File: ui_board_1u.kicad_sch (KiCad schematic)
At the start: 38 parts, among them J1 X9555WV-2x06-6TV01, U1 AFC01-S30FCA-00, U2 SPX3819M5-L, U3 TPS61040DBV

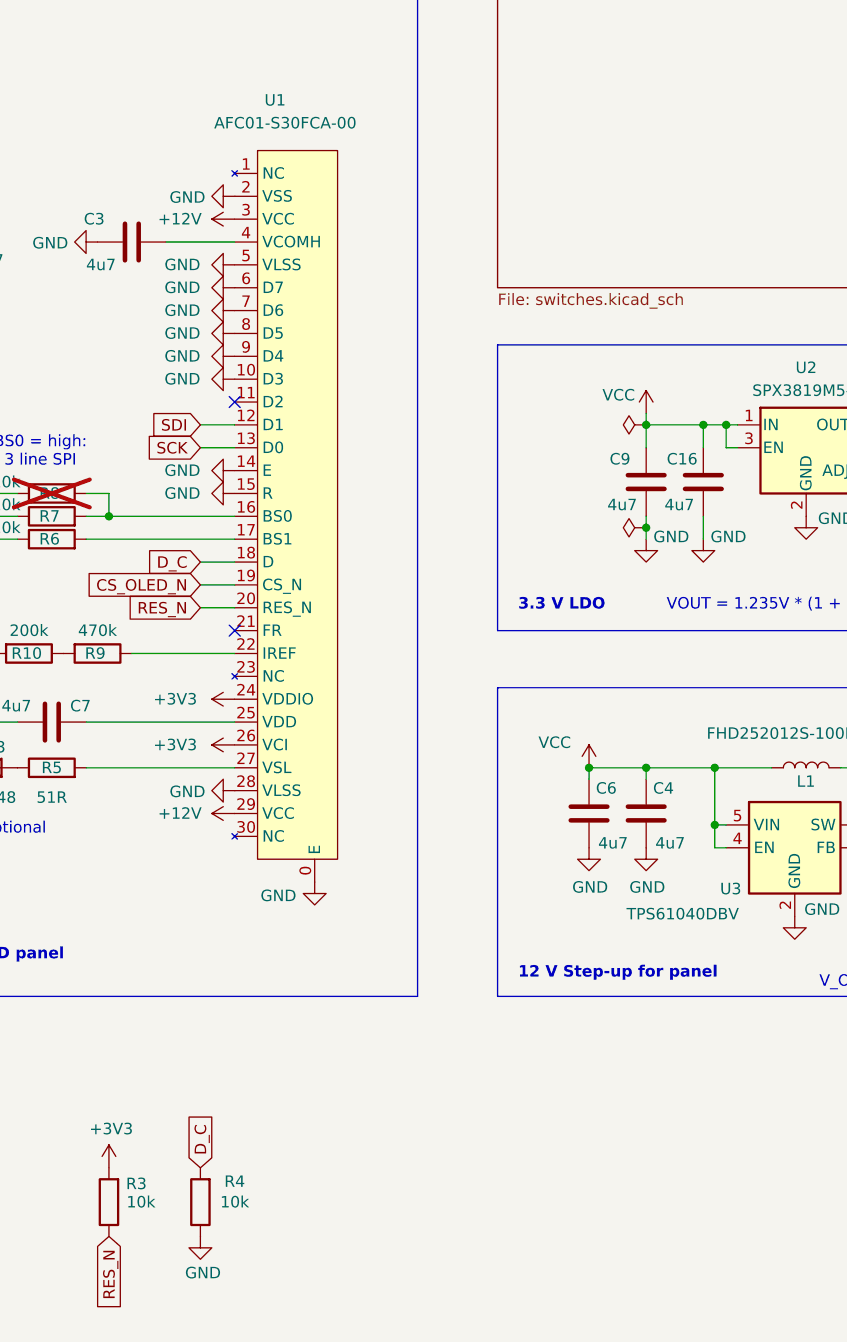
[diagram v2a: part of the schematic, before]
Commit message: review OLED pinout, add 2 GND pins
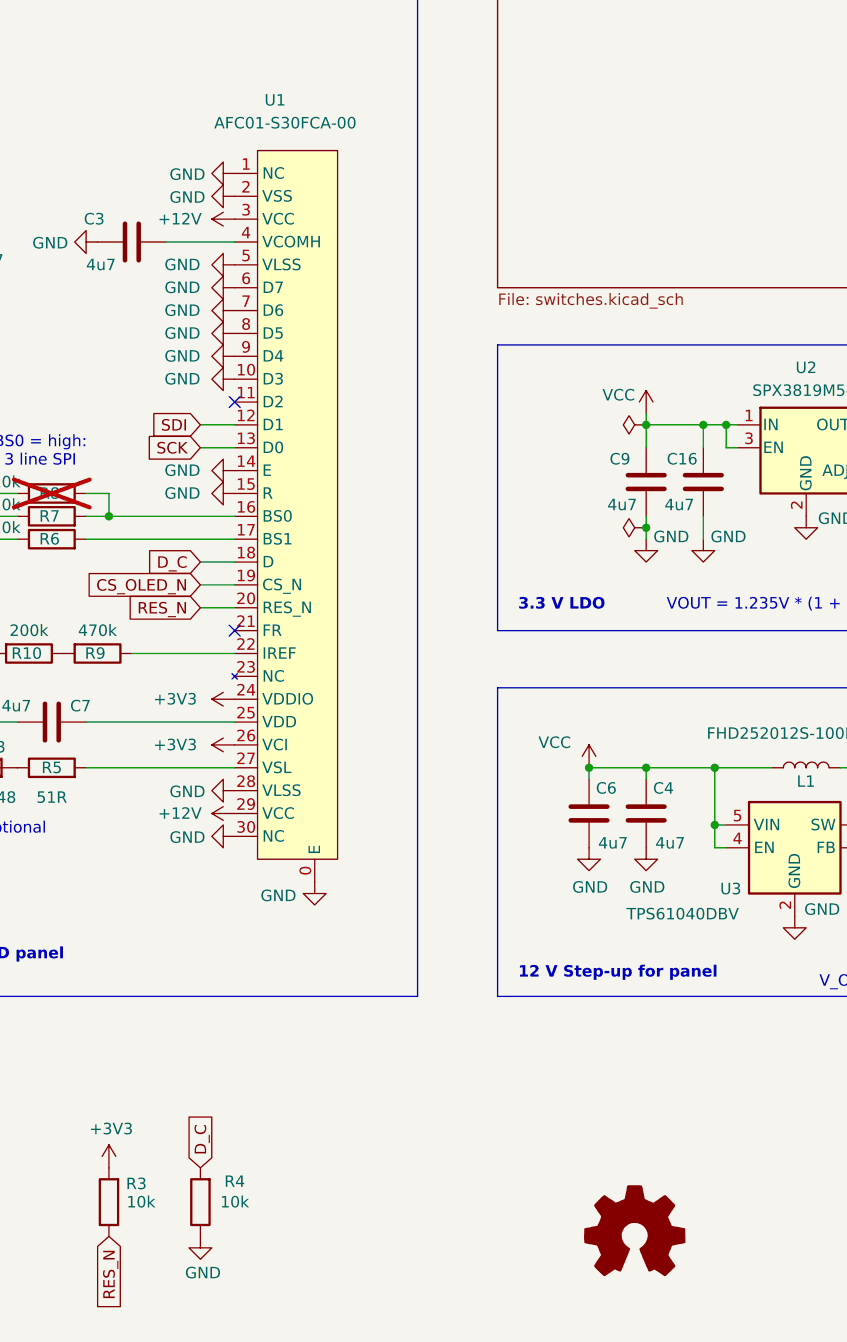
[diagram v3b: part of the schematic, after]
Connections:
- net GND: now also U1.1 (NC), U1.30 (NC)
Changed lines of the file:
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@@
 	(title_block
 		(title "ui_board_1u - User interface board")
-		(date "2025-12-07")
+		(date "2025-12-17")
 		(rev "-")
 		(company "Betz Engineering")
@@
 	)
 	(image
-		(at 182.88 172.72)
+		(at 187.325 172.085)
 		(scale 0.417576)
 		(data "iVBORw0KGgoAAAANSUhEUgAAAP4AAAD+CAYAAAAalrhRAAAACXBIWXMAAC4jAAAuIwF4pT92AAAA"
@@
 	(symbol
 		(lib_id "power:GND")
+		(at 158.75 128.27 270)
+		(unit 1)
+		(exclude_from_sim no)
+		(in_bom yes)
+		(on_board yes)
+		(dnp no)
+		(property "Reference" "#PWR014"
+			(at 152.4 128.27 0)
+			(effects
+				(font
+					(size 1.27 1.27)
+				)
+				(hide yes)
+			)
+		)
+		(property "Value" "GND"
+			(at 155.4988 128.397 90)
+			(effects
+				(font
+					(size 1.27 1.27)
+				)
+				(justify right)
+			)
+		)
+		(property "Footprint" ""
+			(at 158.75 128.27 0)
+			(effects
+				(font
+					(size 1.27 1.27)
+				)
+				(hide yes)
+			)
+		)
+		(property "Datasheet" ""
+			(at 158.75 128.27 0)
+			(effects
+				(font
+					(size 1.27 1.27)
+				)
+				(hide yes)
+			)
+		)
+		(property "Description" ""
+			(at 158.75 128.27 0)
+			(effects
+				(font
+					(size 1.27 1.27)
+				)
+			)
+		)
+		(pin "1"
+		)
+		(instances
+			(project "ui_board_1u"
+				(path "/3def8ca7-c7ff-40fd-acc8-d6d3f6c3eb5b"
+					(reference "#PWR014")
+					(unit 1)
+				)
+			)
+		)
+	)
+	(symbol
+		(lib_id "power:GND")
 		(at 167.64 133.35 0)
 		(unit 1)
@@
 	)
 	(symbol
+		(lib_id "power:GND")
+		(at 158.75 54.61 270)
+		(unit 1)
+		(exclude_from_sim no)
+		(in_bom yes)
+		(on_board yes)
+		(dnp no)
+		(property "Reference" "#PWR013"
+			(at 152.4 54.61 0)
+			(effects
+				(font
+					(size 1.27 1.27)
+				)
+				(hide yes)
+			)
+		)
+		(property "Value" "GND"
+			(at 155.4988 54.737 90)
+			(effects
+				(font
+					(size 1.27 1.27)
+				)
+				(justify right)
+			)
+		)
+		(property "Footprint" ""
+			(at 158.75 54.61 0)
+			(effects
+				(font
+					(size 1.27 1.27)
+				)
+				(hide yes)
+			)
+		)
+		(property "Datasheet" ""
+			(at 158.75 54.61 0)
+			(effects
+				(font
+					(size 1.27 1.27)
+				)
+				(hide yes)
+			)
+		)
+		(property "Description" ""
+			(at 158.75 54.61 0)
+			(effects
+				(font
+					(size 1.27 1.27)
+				)
+			)
+		)
+		(pin "1"
+		)
+		(instances
+			(project "ui_board_1u"
+				(path "/3def8ca7-c7ff-40fd-acc8-d6d3f6c3eb5b"
+					(reference "#PWR013")
+					(unit 1)
+				)
+			)
+		)
+	)
+	(symbol
 		(lib_id "Device:C")
 		(at 248.92 125.73 0)
@@
 					(unit 1)
 				)
+			)
+		)
+	)
+	(symbol
+		(lib_id "Graphic:Logo_Open_Hardware_Small")
+		(at 203.2 172.72 0)
+		(unit 1)
+		(exclude_from_sim yes)
+		(in_bom no)
+		(on_board no)
+		(dnp no)
+		(fields_autoplaced yes)
+		(property "Reference" "#SYM1"
+			(at 203.2 165.735 0)
+			(effects
+				(font
+					(size 1.27 1.27)
+				)
+				(hide yes)
+			)
+		)
+		(property "Value" "Logo_Open_Hardware_Small"
+			(at 203.2 178.435 0)
+			(effects
+				(font
+					(size 1.27 1.27)
+				)
+				(hide yes)
+			)
+		)
+		(property "Footprint" ""
+			(at 203.2 172.72 0)
+			(effects
+				(font
+					(size 1.27 1.27)
+				)
+				(hide yes)
+			)
+		)
+		(property "Datasheet" "~"
+			(at 203.2 172.72 0)
+			(effects
+				(font
+					(size 1.27 1.27)
+				)
+				(hide yes)
+			)
+		)
+		(property "Description" "Open Hardware logo, small"
+			(at 203.2 172.72 0)
+			(effects
+				(font
+					(size 1.27 1.27)
+				)
+				(hide yes)
+			)
+		)
+		(instances
+			(project ""
+				(path "/3def8ca7-c7ff-40fd-acc8-d6d3f6c3eb5b"
+					(reference "#SYM1")
+					(unit 1)
+				)

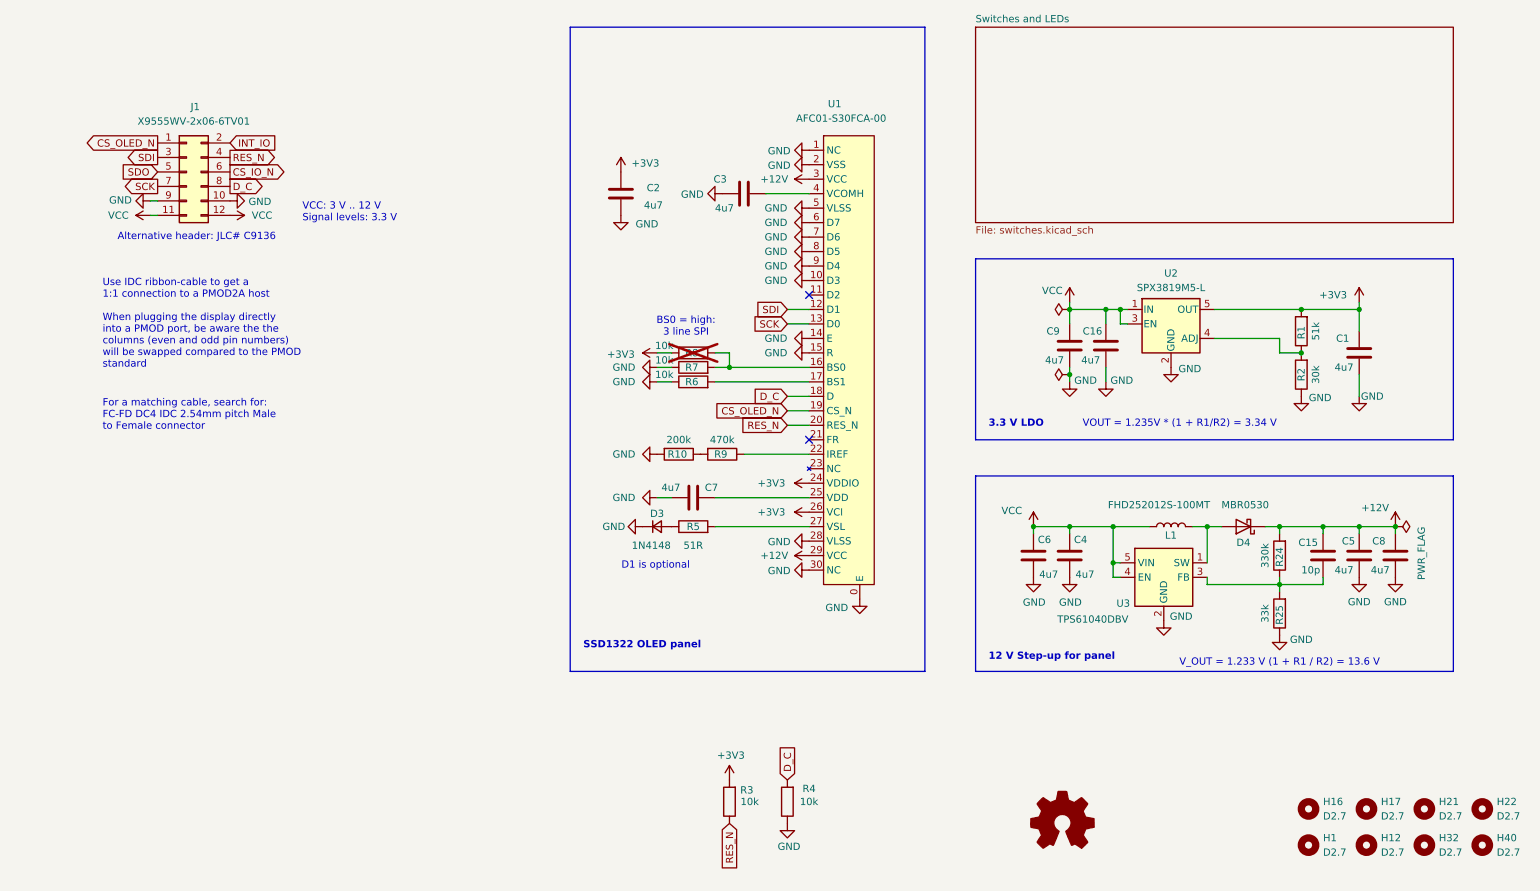
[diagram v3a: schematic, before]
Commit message: add extension board connector
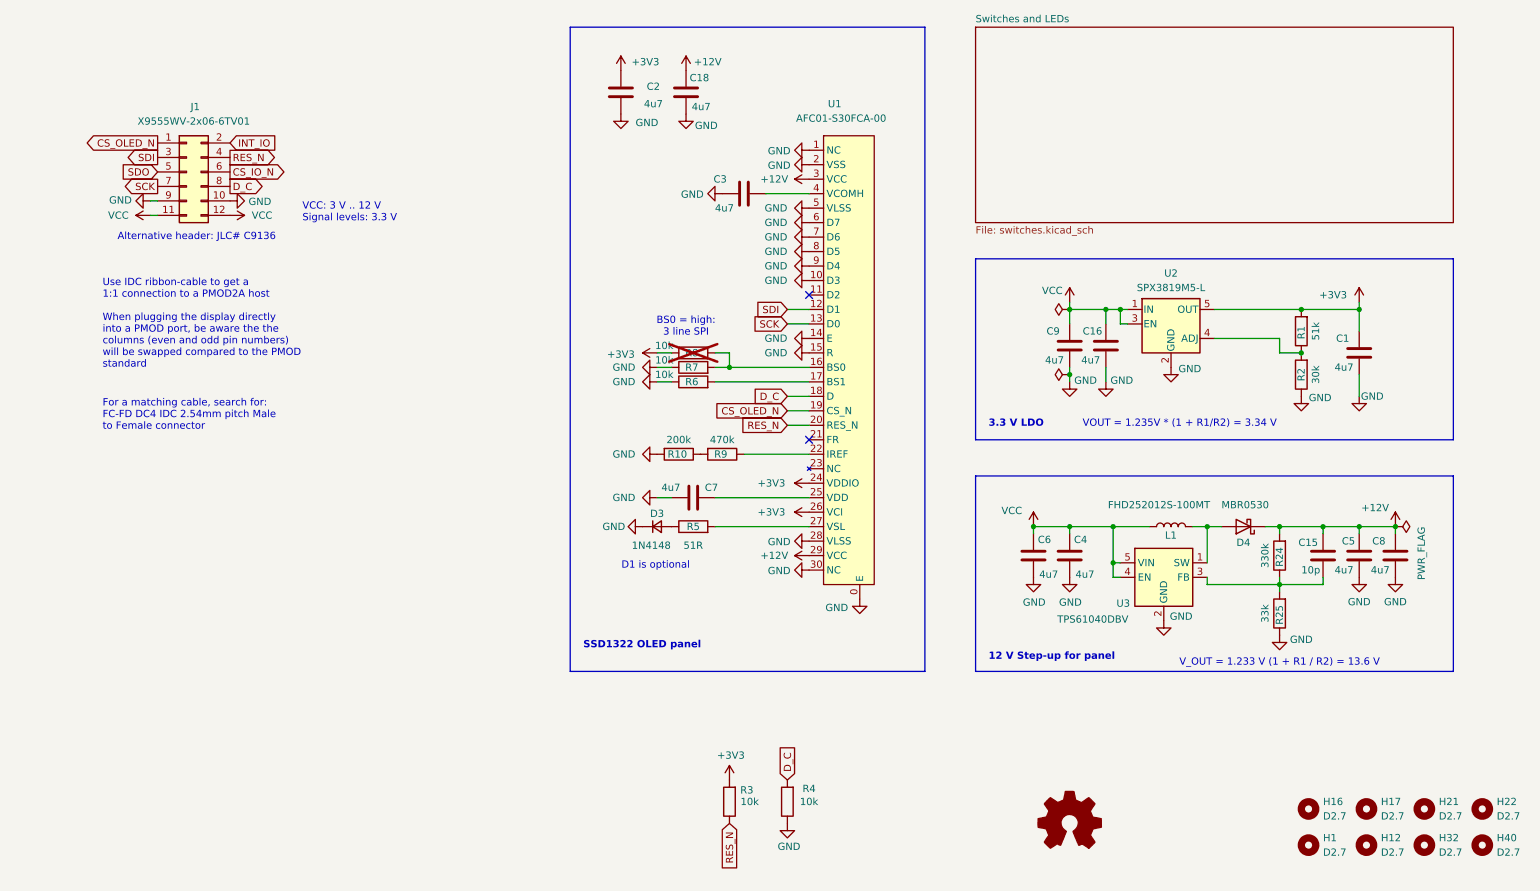
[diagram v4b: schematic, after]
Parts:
- added C18: 4u7, Capacitor_SMD:C_1206_3216Metric, symbol Device:C
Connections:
- net +12V: now also C18.1
- net GND: now also C18.2
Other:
- moved on the sheet: C2

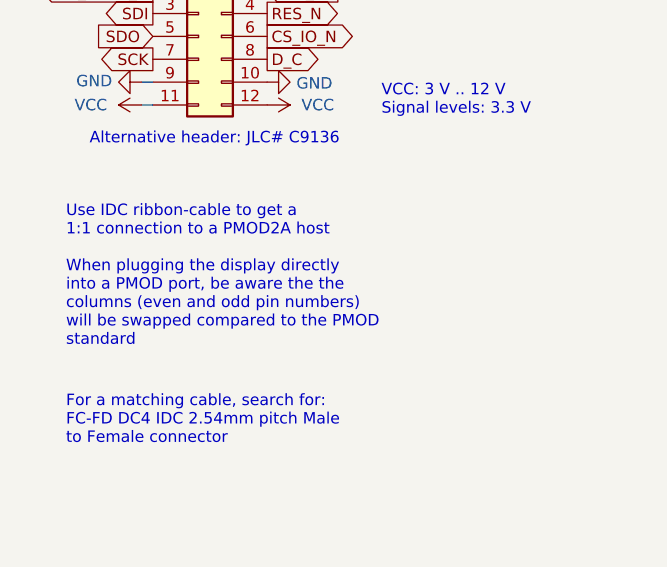
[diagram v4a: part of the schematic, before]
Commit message: fix typo in schematic
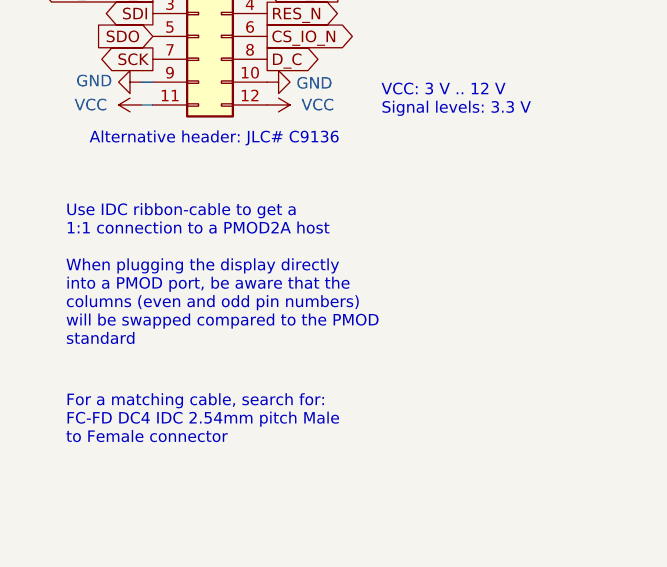
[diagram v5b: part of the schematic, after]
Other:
- note added: "Use IDC ribbon-cable to get a 1:1 connection to a PMOD2A host When plugging the display directly into a PMOD port, be aware that the columns (even and odd pin numbers) will be swapped compared to the PMOD standard"
- note removed: "Use IDC ribbon-cable to get a 1:1 connection to a PMOD2A host When plugging the display directly into a PMOD port, be aware the the columns (even and odd pin numbers) will be swapped compared to the PMOD standard"
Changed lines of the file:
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@@
 		)
 	)
-	(text "Use IDC ribbon-cable to get a \n1:1 connection to a PMOD2A host\n\nWhen plugging the display directly\ninto a PMOD port, be aware the the\ncolumns (even and odd pin numbers)\nwill be swapped compared to the PMOD\nstandard\n\n"
+	(text "Use IDC ribbon-cable to get a \n1:1 connection to a PMOD2A host\n\nWhen plugging the display directly\ninto a PMOD port, be aware that the\ncolumns (even and odd pin numbers)\nwill be swapped compared to the PMOD\nstandard\n\n"
 		(exclude_from_sim no)
 		(at 34.798 86.106 0)
@@
 			"vwAAAIAAAAAAAACAvwAUikCdUcXA3r+JPSuni0BersfA3r+JPSuni0CdUcXA3r+JPQAAAAAAAAAA"
 			"AACAvwAAAAAAAAAAAAAAAAAAAAAAAAAAAAAAAP///////////////wAAAIAAAACA3r+JPQIAAABx"
-			"vFjBAAAAAHeNog=="
-		)
-	)
+			"vFjBAAAAAHeNogAAAAAAAAAAAAAAAAAAAAAAAAAAAAAAAAAAAAAAAAAAAAAAAAAAAAAAAAAAAAAA"
+			"AAAAAAAAAAAAAAAAAAAAAAAAAAAAAAAAAAAAAAAAAAAAAAAAAAAAAAAAAAAAAAAAAAAAAAAAAAAA"
+			"AAAAAAAAAAAAAAAAAAAAAAAAAAAAAAAAAAAAAAAAAAAAAAAAAAAAAAAAAAAAAAAAAAAAAAAAAAAA"
+			"AAAAAAAAAAAAAAAAAAAAAAAAAAAAAAAAAAAAAAAAAAAAAAAAAAAAAAAAAAAAAAAAAAAAAAAAAAAA"
+			"AAAAAAAAAAAAAAAAAAAAAAAAAAAAAAAAAAAAAAAAAAAAAAAAAAAAAAAAAAAAAAAAAAAAAAAAAAAA"
+			"AAAAAAAAAAAAAAAAAAAAAAAAAAAAAAAAAAAAAAAAAAAAAAAAAAAAAAAAAAAAAAAAAAAAAAAAAAAA"
+			"AAAAAAAAAAAAAAAAAAAAAAAAAAAAAAAAAAAAAAAAAAAAAAAAAAAAAAAAAAAAAAAAAAAAAAAAAAAA"
+			"AAAAAAAAAAAAAAAAAAAAAAAAAAAAAAAAAAAAAAAAAAAAAAAAAAAAAAAAAAAAAAAAAAAAAAAAAAAA"
+			"AAAAAAAAAAAAAAAAAAAAAAAAAAAAAAAAAAAAAAAAAAAAAAAAAAAAAAAAAAAAAAAAAAAAAAAAAAAA"
+			"AAAAAAAAAAAAAAAAAAAAAAAAAAAAAAAAAAAAAAAAAAAAAAAAAAAAAAAAAAAAAAAAAAAAAAAAAAAA"
+			"AAAAAAAAAAAAAAAAAAAAAAAAAAAAAAAAAAAAAAAAAAAAAAAAAAAAAAAAAAAAAAAAAAAAAAAAAAAA"
+			"AAAAAAAAAAAAAAAAAAAAAAAAAAAAAAAAAAAAAAAAAAAAAAAAAAAAAAAAAAAAAAAAAAAAAAAAAAAA"
+			"AAAAAAAAAAAAAAAAAAAAAAAAAAAAAAAAAAAAAAAAAAAAAAAAAAAAAAAAAAAAAAAAAAAAAAAAAAAA"
+			"AAAAAAAAAAAAAAAAAAAAAAAAAAAAAAAAAAAAAAAAAAAAAAAAAAAAAAAAAAAAAAAAAAAAAAAAAAAA"
+			"AAAAAAAAAAAAAAAAAAAAAAAAAAAAAAAAAAAAAAAAAAAAAAAAAAAAAAAAAAAAAAAAAAAAAAAAAAAA"
+			"AAAAAAAAAAAAAAAAAAAAAAAAAAAAAAAAAAAAAAAAAAAAAAAAAAAAAAAAAAAAAAAAAAAAAAAAAAAA"
+			"AAAAAAAAAAAAAAAAAAAAAAAAAAAAAAAAAAAAAAAAAAAAAAAAAAAAAAAAAAAAAAAAAAAAAAAAAAAA"
+			"AAAAAAAAAAAAAAAAAAAAAAAAAAAAAAAAAAAAAAAAAAAAAAAAAAAAAAAAAAAAAAAAAAAAAAAAAAAA"
+			"AAAAAAAAAAAAAA=="
+		)
+	)
